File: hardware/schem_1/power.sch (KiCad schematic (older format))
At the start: 18 parts

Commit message: update schematic: add io expander with peripherals, update power circuitry- change some components. update project plan. update footprints
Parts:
- removed U?: XC6222D331MR-G, symbol schem_1-cache:XC6222D331MR-G
- added C23: 10uF, Capacitor_SMD:C_0805_2012Metric, symbol Device:C_Small
- added C24: 1uF, Capacitor_SMD:C_0603_1608Metric, symbol Device:C_Small
- added C9: 1uF ceramic, Capacitor_SMD:C_0603_1608Metric, symbol Device:C_Small
- added D3: LED_GREEN, LED_SMD:LED_0805_2012Metric, symbol Device:LED
- added R16: 130, symbol Device:R
- added U3: Latch_Switch, symbol jclib:Latch_Switch
- added U9: XC6210B332MR-DigikeyJc, Package_TO_SOT_SMD:SOT-23-5, symbol xc6210b332mr-digikeyjc:XC6210B332MR-DigikeyJc
- C10, C14, C16: renamed from C?; footprint (none) -> Capacitor_SMD:C_0805_2012Metric
- C11, C15: renamed from C?; footprint (none) -> Capacitor_SMD:C_0603_1608Metric
- C12: renamed from C?; value 1uF ceramic -> 1uF; footprint (none) -> Capacitor_SMD:C_0603_1608Metric
- C13: renamed from C?; value 1F -> FGH0H105ZF; footprint (none) -> kicad_lib:CP_Radial_FGH0H105ZF‎
- C8: renamed from C?; value 10uF -> 10uF DNF; footprint (none) -> Capacitor_SMD:C_0805_2012Metric
- D1, D2: renamed from D?; value D_Schottky -> PMEG2005EGWX; footprint (none) -> Diode_SMD:D_SOD-123
- J3: renamed from J?; footprint (none) -> Digikey:USB_Mini_B_Female_UJ2-MBH-1-SMT-TR
- Q1: renamed from Q?; value Q_PMOS_DGS -> NDS332P; footprint (none) -> Package_TO_SOT_SMD:SuperSOT-3
- R18: renamed from R?; value 24R 3W -> CRCW251224R0JNEG; footprint (none) -> Resistor_SMD:R_2512_6332Metric
- gave numbers to parts that had none: 4
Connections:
- wire segments 63 -> 77
- no-connect marks 1 -> 3
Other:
- moved on the sheet: C10, C11, C12, C13, C14, C15, C16, C8, D1, D2, Q1, R17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

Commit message: Replace ESP32 Wroom module with WRover and remove the external PSRAM (as Wrover has one built in). Create symbol and footprint for Wrover. Update footprints for resistors and buttons. Update USB footprint as it was not matching symbol.
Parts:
- removed U3: Latch_Switch, symbol jclib:Latch_Switch
- removed U9: XC6210B332MR-DigikeyJc, Package_TO_SOT_SMD:SOT-23-5, symbol xc6210b332mr-digikeyjc:XC6210B332MR-DigikeyJc
- added SW3: SW_SPDT, Button_Switch_THT:SW_E-Switch_EG1224_SPDT_Angled, symbol Switch:SW_SPDT
- added U2: XC6210B332MR, Package_TO_SOT_SMD:SOT-23-5, symbol Regulator_Linear:XC6210B332MR
- C9: value 1uF ceramic -> 1uF
- R16, R17, R19: footprint (none) -> Resistor_SMD:R_0603_1608Metric
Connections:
- wire segments 77 -> 76
- no-connect marks 3 -> 2
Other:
- moved on the sheet: C10, C11, C14, C15, C16, C23, C24, C8, D3, Q1, R16, R17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

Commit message: change supercap for one with lower esr and shorter. create footprint and 3d model for new cap. remove power switch entirely.
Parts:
- removed C13: FGH0H105ZF, kicad_lib:CP_Radial_FGH0H105ZF‎, symbol Device:CP
- removed SW3: SW_SPDT, Button_Switch_THT:SW_E-Switch_EG1224_SPDT_Angled, symbol Switch:SW_SPDT
- added C2: DGH105Q5R5, kicad_lib:DGH105Q5R5-Horizontal, symbol Device:CP
- added R5: 0R DNF, Resistor_SMD:R_0603_1608Metric, symbol Device:R_Small
- J3: footprint Digikey:USB_Mini_B_Female_UJ2-MBH-1-SMT-TR -> kicad_lib:USB_Mini_B_Female_UJ2-MBH-1-SMT-TR-JC
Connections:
- wire segments 76 -> 77
- no-connect marks 2 -> 1

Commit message: update footprints for 24way connector, 3D models. add new connector to connect the two PCB's
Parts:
- removed J3: USB_B_Mini, kicad_lib:USB_Mini_B_Female_UJ2-MBH-1-SMT-TR-JC, symbol Connector:USB_B_Mini
- added J5: UJ2-MBH-1-SMT, UJ2-MBH-1-SMT:CUI_UJ2-MBH-1-SMT, symbol UJ2-MBH-1-SMT:UJ2-MBH-1-SMT
- R5: value 0R DNF -> 0R; DNF (none) -> DNF
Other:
- note added: "USB Mini"
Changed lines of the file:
@@
 L power:GND #PWR?
 U 1 1 6169C4E5
-P 2055 3875
+P 2430 3965
 AR Path="/6169C4E5" Ref="#PWR?"  Part="1"
 AR Path="/616783E5/6169C4E5" Ref="#PWR032"  Part="1"
-F 0 "#PWR032" H 2055 3625 50  0001 C CNN
-F 1 "GND" H 2060 3702 50  0000 C CNN
-F 2 "" H 2055 3875 50  0001 C CNN
-F 3 "" H 2055 3875 50  0001 C CNN
-	1    2055 3875
+F 0 "#PWR032" H 2430 3715 50  0001 C CNN
+F 1 "GND" H 2435 3792 50  0000 C CNN
+F 2 "" H 2430 3965 50  0001 C CNN
+F 3 "" H 2430 3965 50  0001 C CNN
+	1    2430 3965
 	1    0    0    -1
 $EndComp
-NoConn ~ 2355 3575
-Wire Wire Line
-	2055 3775 2055 3825
-Wire Wire Line
-	1955 3775 1955 3825
-Wire Wire Line
-	1955 3825 2055 3825
-Connection ~ 2055 3825
-Wire Wire Line
-	2055 3825 2055 3875
-$Comp
-L Connector:USB_B_Mini J?
-U 1 1 60BF6967
-P 2055 3375
-AR Path="/60BF6967" Ref="J?"  Part="1"
-AR Path="/616783E5/60BF6967" Ref="J3"  Part="1"
-F 0 "J3" H 2112 3842 50  0000 C CNN
-F 1 "USB_B_Mini" H 2112 3751 50  0000 C CNN
-F 2 "kicad_lib:USB_Mini_B_Female_UJ2-MBH-1-SMT-TR-JC" H 2205 3325 50  0001 C CNN
-F 3 "~" H 2205 3325 50  0001 C CNN
-	1    2055 3375
-	1    0    0    -1
-$EndComp
+NoConn ~ 2350 3475
 $Comp
 L Device:R_Small R5
 U 1 1 60BFC311
 P 2510 3375
-F 0 "R5" V 2314 3375 50  0000 C CNN
-F 1 "0R DNF" V 2405 3375 50  0000 C CNN
+F 0 "R5" V 2515 3375 50  0000 C CNN
+F 1 "0R" V 2445 3370 50  0000 C CNN
 F 2 "Resistor_SMD:R_0603_1608Metric" H 2510 3375 50  0001 C CNN
 F 3 "~" H 2510 3375 50  0001 C CNN
+F 4 "DNF" V 2585 3380 50  0000 C CNN "DNF"
 	1    2510 3375
 	0    1    1    0
 $EndComp
 Wire Wire Line
-	2355 3375 2410 3375
+	2630 3375 2610 3375
+Connection ~ 2825 3175
+$Comp
+L UJ2-MBH-1-SMT:UJ2-MBH-1-SMT J5
+U 1 1 60BD2726
+P 1950 3475
+F 0 "J5" H 2057 4132 50  0000 C CNN
+F 1 "UJ2-MBH-1-SMT" H 2057 4041 50  0000 C CNN
+F 2 "UJ2-MBH-1-SMT:CUI_UJ2-MBH-1-SMT" H 2057 3950 50  0000 C CNN
+F 3 "" H 1950 3475 50  0001 L BNN
+F 4 "CUI INC" H 1950 3475 50  0001 L BNN "MANUFACTURER"
+F 5 "MANUFACTURER RECOMMENDATION" H 1950 3475 50  0001 L BNN "STANDARD"
+F 6 "1.0" H 1950 3475 50  0001 L BNN "PART_REV"
+	1    1950 3475
+	1    0    0    -1
+$EndComp
 Wire Wire Line
-	2355 3475 2630 3475
+	2350 3175 2825 3175
 Wire Wire Line
-	2630 3475 2630 3375
+	2630 3275 2630 3375
 Wire Wire Line
-	2630 3375 2610 3375
+	2350 3275 2630 3275
 Wire Wire Line
-	2350 3175 2355 3175
-Connection ~ 2825 3175
-Connection ~ 2355 3175
+	2350 3375 2410 3375
 Wire Wire Line
-	2355 3175 2825 3175
+	2350 3575 2430 3575
+Connection ~ 2430 3965
+Wire Wire Line
+	2430 3965 2430 3970
+Wire Wire Line
+	2350 3775 2430 3775
+Wire Wire Line
+	2430 3575 2430 3775
+Connection ~ 2430 3775
+Wire Wire Line
+	2430 3775 2430 3965
+Text Notes 1690 3605 1    50   ~ 0
+USB Mini
 $EndSCHEMATC

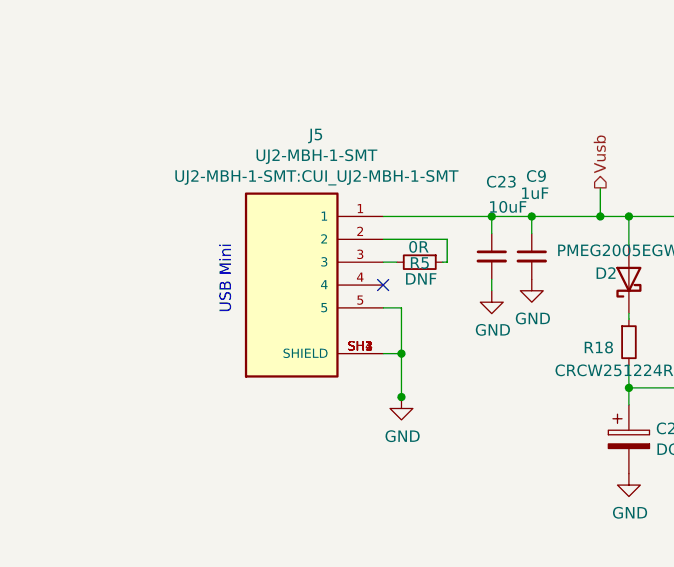
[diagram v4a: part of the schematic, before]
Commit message: add correct 3d model for esp32 wrover e. initial placement of components done for both boards. need to start routing
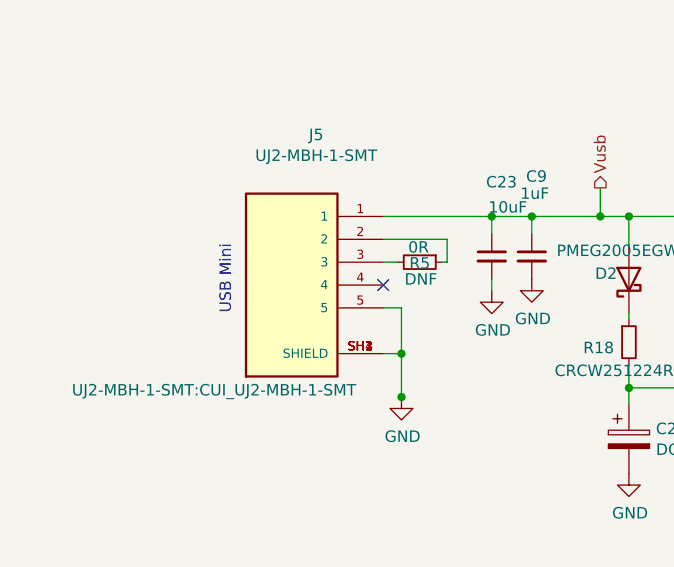
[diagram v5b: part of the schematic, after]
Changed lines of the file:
@@
 	4450 3350 4450 3175
-Wire Wire Line
-	4025 3175 4450 3175
 Wire Wire Line
 	3425 3300 3425 3175
@@
 Wire Wire Line
 	2630 3375 2610 3375
-Connection ~ 2825 3175
 $Comp
 L UJ2-MBH-1-SMT:UJ2-MBH-1-SMT J5
@@
 F 0 "J5" H 2057 4132 50  0000 C CNN
 F 1 "UJ2-MBH-1-SMT" H 2057 4041 50  0000 C CNN
-F 2 "UJ2-MBH-1-SMT:CUI_UJ2-MBH-1-SMT" H 2057 3950 50  0000 C CNN
+F 2 "UJ2-MBH-1-SMT:CUI_UJ2-MBH-1-SMT" H 1610 3015 50  0000 C CNN
 F 3 "" H 1950 3475 50  0001 L BNN
 F 4 "CUI INC" H 1950 3475 50  0001 L BNN "MANUFACTURER"
@@
 	1    0    0    -1
 $EndComp
-Wire Wire Line
-	2350 3175 2825 3175
 Wire Wire Line
 	2630 3275 2630 3375
@@
 Text Notes 1690 3605 1    50   ~ 0
 USB Mini
+Connection ~ 2825 3175
+Wire Wire Line
+	2350 3175 2825 3175
+Wire Wire Line
+	4025 3175 4450 3175
 $EndSCHEMATC

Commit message: update to latest gerbers, update project plan
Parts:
- C10, C14, C16, C23: LCSC (none) -> C15850
- C11, C15: LCSC (none) -> C268011
- C12, C24, C9: LCSC (none) -> C15849
- D3: LCSC (none) -> C63855
- R16: LCSC (none) -> C228126
- R17: LCSC (none) -> C25804
- R19: LCSC (none) -> C21190
- U2: LCSC (none) -> C47719
- U5: LCSC (none) -> C2827652
- U6: LCSC (none) -> C424699
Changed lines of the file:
@@
 F 2 "Package_TO_SOT_SMD:SOT-23-5" H 5425 3275 50  0001 C CNN
 F 3 "https://www.torexsemi.com/file/xc6210/XC6210.pdf" H 6175 2275 50  0001 C CNN
+F 4 "C47719" H 5425 3275 50  0001 C CNN "LCSC"
 	1    5425 3275
 	1    0    0    -1
@@
 F 2 "Capacitor_SMD:C_0603_1608Metric" H 6175 3325 50  0001 C CNN
 F 3 "~" H 6175 3325 50  0001 C CNN
+F 4 "C15849" H 6175 3325 50  0001 C CNN "LCSC"
 	1    6175 3325
 	1    0    0    -1
@@
 F 2 "Package_TO_SOT_SMD:SOT-23" H 8750 4250 50  0001 C CIN
 F 3 "https://www.torexsemi.com/file/xc6206/XC6206.pdf" H 8750 4025 50  0001 C CNN
+F 4 "C424699" H 8750 4025 50  0001 C CNN "LCSC"
 	1    8750 4025
 	1    0    0    -1
@@
 F 2 "Package_TO_SOT_SMD:SOT-23" H 8750 3400 50  0001 C CIN
 F 3 "https://www.torexsemi.com/file/xc6206/XC6206.pdf" H 8750 3175 50  0001 C CNN
+F 4 "C2827652" H 8750 3175 50  0001 C CNN "LCSC"
 	1    8750 3175
 	1    0    0    -1
@@
 F 2 "Resistor_SMD:R_0603_1608Metric" V 7980 3925 50  0001 C CNN
 F 3 "~" H 8050 3925 50  0001 C CNN
+F 4 "C21190" H 8050 3925 50  0001 C CNN "LCSC"
 	1    8050 3925
 	1    0    0    -1
@@
 F 2 "Capacitor_SMD:C_0805_2012Metric" H 8350 4425 50  0001 C CNN
 F 3 "~" H 8350 4425 50  0001 C CNN
+F 4 "C15850" H 8350 4425 50  0001 C CNN "LCSC"
 	1    8350 4425
 	1    0    0    -1
@@
 F 2 "Capacitor_SMD:C_0805_2012Metric" H 9250 3375 50  0001 C CNN
 F 3 "~" H 9250 3375 50  0001 C CNN
+F 4 "C15850" H 9250 3375 50  0001 C CNN "LCSC"
 	1    9250 3375
 	1    0    0    -1
@@
 F 2 "Resistor_SMD:R_0603_1608Metric" V 7580 3475 50  0001 C CNN
 F 3 "~" H 7650 3475 50  0001 C CNN
+F 4 "C25804" H 7650 3475 50  0001 C CNN "LCSC"
 	1    7650 3475
 	1    0    0    -1
@@
 F 2 "Capacitor_SMD:C_0603_1608Metric" H 9650 3375 50  0001 C CNN
 F 3 "~" H 9650 3375 50  0001 C CNN
+F 4 "C268011" H 9650 3375 50  0001 C CNN "LCSC"
 	1    9650 3375
 	1    0    0    -1
@@
 F 2 "Capacitor_SMD:C_0805_2012Metric" H 9250 4225 50  0001 C CNN
 F 3 "~" H 9250 4225 50  0001 C CNN
+F 4 "C15850" H 9250 4225 50  0001 C CNN "LCSC"
 	1    9250 4225
 	1    0    0    -1
@@
 F 2 "Capacitor_SMD:C_0603_1608Metric" H 9650 4225 50  0001 C CNN
 F 3 "~" H 9650 4225 50  0001 C CNN
+F 4 "C268011" H 9650 4225 50  0001 C CNN "LCSC"
 	1    9650 4225
 	1    0    0    -1
@@
 F 2 "LED_SMD:LED_0805_2012Metric" H 7075 3725 50  0001 C CNN
 F 3 "~" H 7075 3725 50  0001 C CNN
+F 4 "C63855" V 7075 3725 50  0001 C CNN "LCSC"
 	1    7075 3725
 	0    -1   -1   0
@@
 F 2 "Resistor_SMD:R_0603_1608Metric" V 7005 3425 50  0001 C CNN
 F 3 "~" H 7075 3425 50  0001 C CNN
+F 4 "C228126" H 7075 3425 50  0001 C CNN "LCSC"
 	1    7075 3425
 	1    0    0    -1
@@
 F 2 "Capacitor_SMD:C_0805_2012Metric" H 2825 3350 50  0001 C CNN
 F 3 "~" H 2825 3350 50  0001 C CNN
+F 4 "C15850" H 2825 3350 50  0001 C CNN "LCSC"
 	1    2825 3350
 	1    0    0    -1
@@
 F 2 "Capacitor_SMD:C_0603_1608Metric" H 3000 3350 50  0001 C CNN
 F 3 "~" H 3000 3350 50  0001 C CNN
+F 4 "C15849" H 3000 3350 50  0001 C CNN "LCSC"
 	1    3000 3350
 	1    0    0    -1
@@
 F 2 "Capacitor_SMD:C_0603_1608Metric" H 4450 3450 50  0001 C CNN
 F 3 "~" H 4450 3450 50  0001 C CNN
+F 4 "C15849" H 4450 3450 50  0001 C CNN "LCSC"
 	1    4450 3450
 	1    0    0    -1
